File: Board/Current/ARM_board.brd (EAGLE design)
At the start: 105.2 x 84.8 mm, 157 parts, among them IC3 STM32F437VI, IC4 LM358DT, J1 USART/I2C, J10 ANALOG, J11 DGND, J12 DPWR, J13 DIGITAL, J14 SGND, J15 SPWR, J16 SERVO, J2 I2C2/USART3, J3 USART2, J5 SPI, J6 Bluesmirf, J7 SWD, J8 AGND, J9 APWR, Q1 STL4P2UH7, Q2 2STR1230, SW1 SW, U1 LSM330DLC, U10 BAV99, U11 BAV99, U12 USBLC6-2, U13 USBLC6-2, U14 STMPS2171MTR, U15 MC74HC164, U16 STL85N6F3, U17 ZENER-BZX384C20-E3-08, U18 ZENER-BZX384C20-E3-08, U2 RT7259, U3 NC7SZU04, U4 L6206Q, U5 L6206Q, U6 SI7617, U7 SI7617, U8 SI7617, U9 SI7617, Y2 8MHz

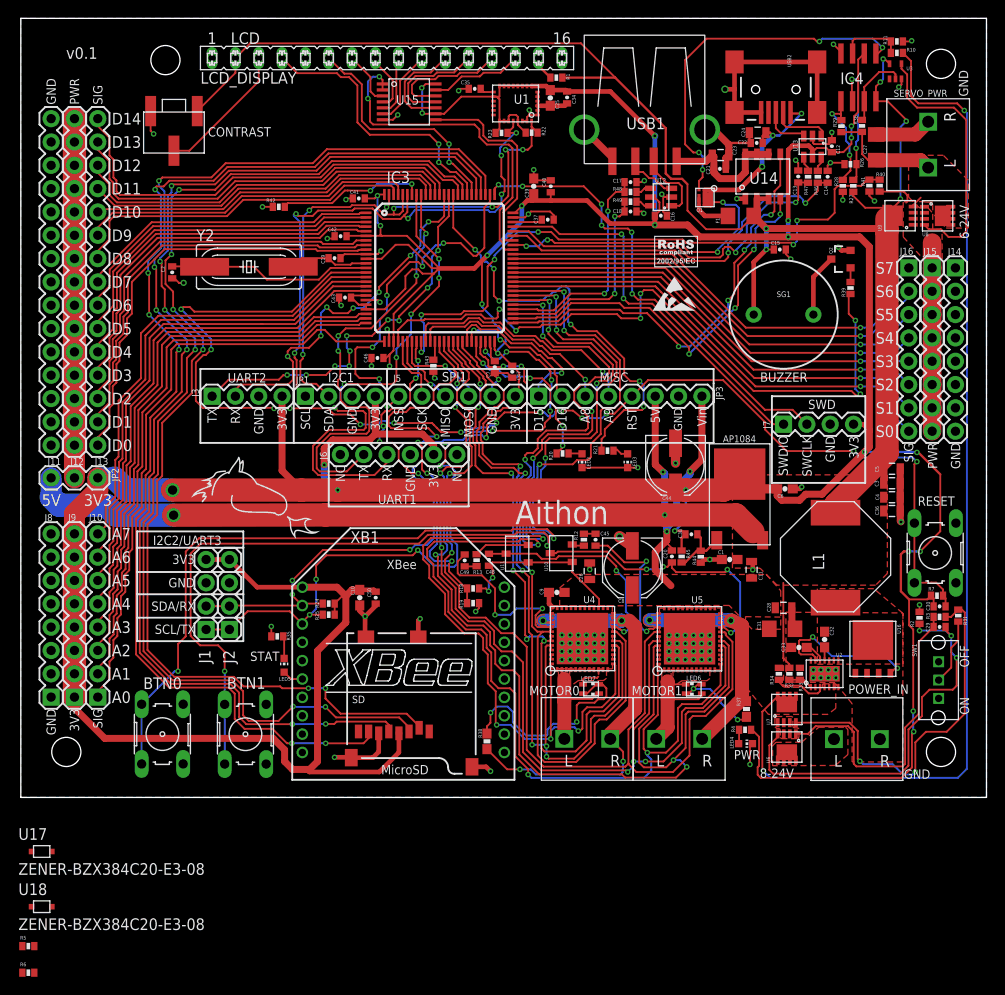
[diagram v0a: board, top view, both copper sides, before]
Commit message: Added green box 30mil inside the board outline and moved all traces within the line. Removed the extra space that was added around the board for the previous revision. Removed the zener diodes for now (need to re-evaluate them).
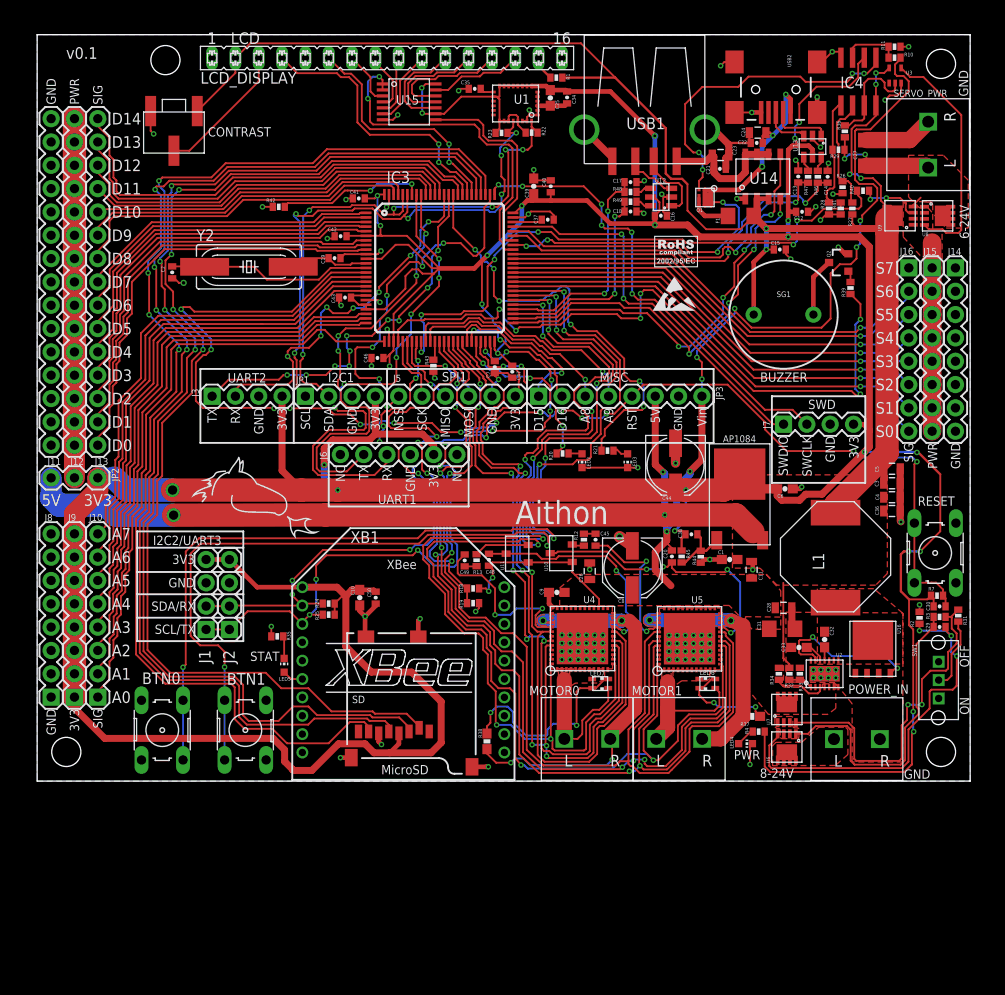
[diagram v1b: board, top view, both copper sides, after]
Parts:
- removed R5, R6: 10k, SparkFun:0402-RES
- removed U17, U18: ZENER-BZX384C20-E3-08, zener-BZX384C20-E3-08:ZENER-BZX384C20-E3-08
- moved C12 7.84 mm to (83.3, 62.0), turned to 0 degrees
- moved R41 3.99 mm to (87.5, 62.4)
- moved R28 2.88 mm to (86.2, 62.4)
- moved R26 2.65 mm to (87.7, 64.7), turned to 90 degrees
- moved R29 2.59 mm to (87.3, 68.8), turned to 180 degrees
- moved R27 2.47 mm to (88.8, 62.4)
- moved R36 1.95 mm to (88.0, 70.8)
- moved R40 1.89 mm to (89.9, 64.3), turned to 180 degrees
- moved LED6 1.58 mm to (73.0, 10.6)
- moved R4 1.50 mm to (78.6, 5.39)
- moved C27 1.24 mm to (90.3, 68.4)
- moved LED7 1.15 mm to (61.3, 10.6)
- moved R37 1.02 mm to (77.9, 7.05), turned to 0 degrees
- moved R11 0.63 mm to (93.4, 80.0)
- moved R10 0.58 mm to (93.4, 78.8)
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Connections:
- net GND: no longer R5.2, R6.2
- net N$30: no longer R6.1, U17.P$2
- net RAW_SPWR: no longer R5.1, U18.P$2
- net SPWR: no longer U17.P$1, U18.P$1
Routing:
- net MPOWER: track 159.5 -> 105.5 mm, vias 6 -> 9
- net GND: track 158.9 -> 140.2 mm, vias 105 -> 109
- net M0_B: track 112.6 -> 106.7 mm
- net +3V3: track 557.9 -> 563.5 mm
- net N$14: track 39.6 -> 34.7 mm
- net N$68: track 40.7 -> 37.0 mm
- net N$30: track 28.9 -> 25.7 mm
- net N$27: track 8.39 -> 11.5 mm
- net SPWR: track 24.6 -> 27.4 mm, vias 0 -> 2
- net OUT4: track 46.2 -> 43.6 mm
- net BTN0: track 111.2 -> 108.6 mm
- net SERVO_SENSE: track 68.4 -> 66.2 mm
- net OUT1: track 14.1 -> 16.2 mm
- net N$52: track 24.7 -> 22.7 mm
- net USB_5V: track 55.9 -> 57.8 mm
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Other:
- board size 105.2 x 84.8 mm -> 101.6 x 81.3 mm

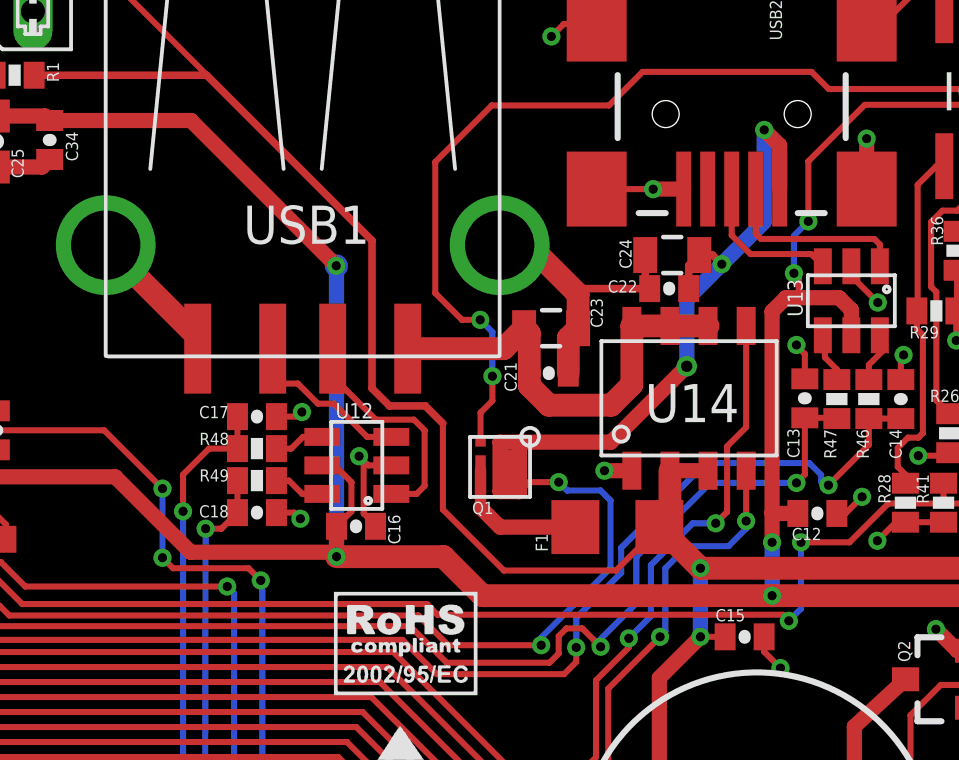
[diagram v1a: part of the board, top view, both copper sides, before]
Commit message: Fixed parts that were too close together.
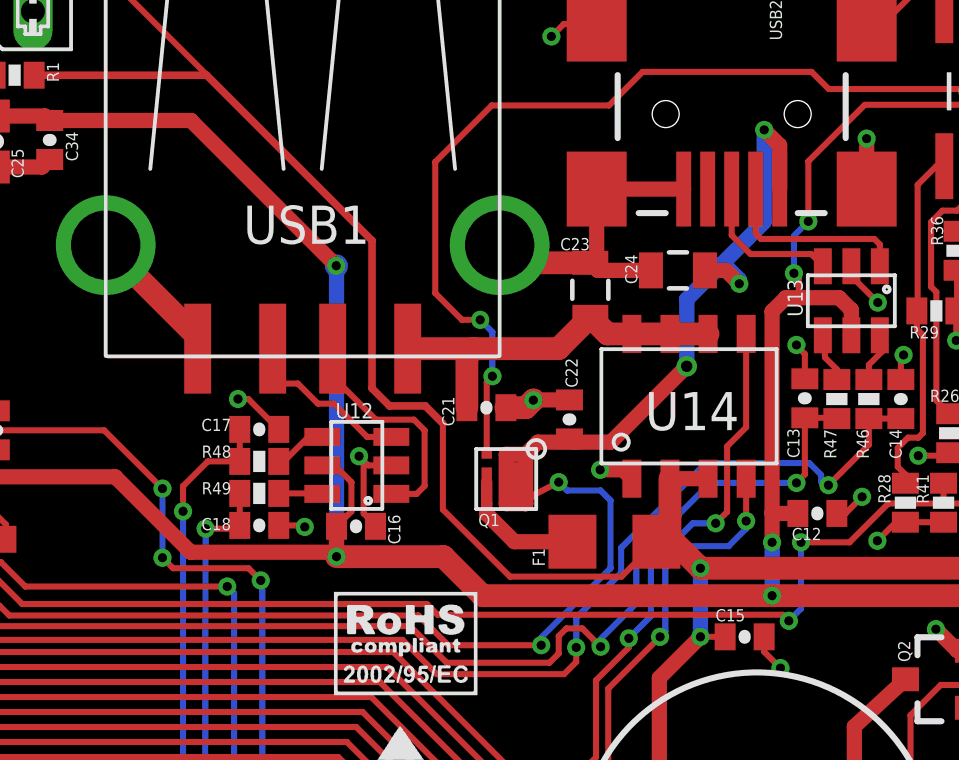
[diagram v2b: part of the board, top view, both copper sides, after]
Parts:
- moved C22 5.48 mm to (75.0, 65.1), turned to 270 degrees
- moved C21 2.38 mm to (72.3, 65.5)
- moved C23 1.83 mm to (75.7, 69.5), turned to 90 degrees
- moved C24 0.54 mm to (78.7, 70.1)
- moved F1 0.50 mm to (75.3, 58.5)
- moved Q1 0.45 mm to (72.9, 63.1)
- moved R49 0.43 mm to (64.7, 62.7)
- moved C17 0.43 mm to (64.7, 64.8)
- moved C18 0.43 mm to (64.7, 61.6)
- moved R48 0.43 mm to (64.7, 63.7)
- moved U14 0.27 mm to (78.4, 64.9)
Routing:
- net N$21: track 14.6 -> 12.8 mm
- net GND: track 140.2 -> 141.8 mm

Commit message: Changed servo power select resistors.
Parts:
- added R5, R6: 100k, SparkFun:0402-RES
- R36: value 10k -> 100k
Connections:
- new net N$50: R5.2, U9.4
- new net N$53: R6.1, U8.4
- net N$30: now also R6.2; no longer U8.4
- net RAW_SPWR: now also R5.1; no longer U9.4
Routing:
- net RAW_SPWR: track 14.2 -> 12.9 mm
- net N$30: track 25.7 -> 25.1 mm
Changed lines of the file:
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@@
 <layer number="39" name="tKeepout" color="4" fill="11" visible="no" active="yes"/>
 <layer number="40" name="bKeepout" color="1" fill="11" visible="no" active="yes"/>
-<layer number="41" name="tRestrict" color="4" fill="10" visible="no" active="yes"/>
+<layer number="41" name="tRestrict" color="4" fill="10" visible="yes" active="yes"/>
 <layer number="42" name="bRestrict" color="1" fill="10" visible="no" active="yes"/>
 <layer number="43" name="vRestrict" color="2" fill="10" visible="yes" active="yes"/>
@@
 <wire x1="100.838" y1="0.762" x2="0.762" y2="0.762" width="0" layer="43"/>
 <wire x1="0.762" y1="0.762" x2="0.762" y2="80.518" width="0" layer="43"/>
+<wire x1="1.27" y1="80.01" x2="100.33" y2="80.01" width="0" layer="43"/>
+<wire x1="100.33" y1="80.01" x2="100.33" y2="1.27" width="0" layer="43"/>
+<wire x1="100.33" y1="1.27" x2="1.27" y2="1.27" width="0" layer="43"/>
+<wire x1="1.27" y1="1.27" x2="1.27" y2="80.01" width="0" layer="43"/>
 </plain>
 <attributes>
@@
 <attribute name="VALUE" x="99.710240625" y="18.912840625" size="0.4064" layer="27" font="vector" rot="R90"/>
 </element>
-<element name="R36" library="SparkFun" package="0402-RES" value="10k" x="87.955121875" y="70.754240625" smashed="yes" rot="R270">
+<element name="R36" library="SparkFun" package="0402-RES" value="100k" x="87.955121875" y="70.754240625" smashed="yes" rot="R270">
 <attribute name="NAME" x="87.4903" y="70.926959375" size="0.4064" layer="25" font="vector" rot="R90"/>
 <attribute name="VALUE" x="87.5385625" y="71.78548125" size="0.4064" layer="27" font="vector"/>
@@
 <attribute name="VALUE" x="48.674021875" y="5.80644375" size="0.4064" layer="27" font="vector"/>
 </element>
+<element name="R5" library="SparkFun" package="0402-RES" value="100k" x="-0.96011875" y="-13.738859375"/>
+<element name="R6" library="SparkFun" package="0402-RES" value="100k" x="-0.96011875" y="-16.634459375"/>
 </elements>
 <signals>
@@
 <contactref element="SERVO_PWR" pad="L"/>
 <contactref element="R36" pad="2"/>
-<contactref element="U9" pad="4"/>
-<contactref element="U8" pad="5"/>
-<contactref element="U8" pad="6"/>
-<contactref element="U8" pad="7"/>
-<contactref element="U8" pad="8"/>
-<contactref element="U8" pad="PAD"/>
 <polygon width="0.0254" layer="1" thermals="no" rank="2">
 <vertex x="94.8944" y="68.1482"/>
@@
 <vertex x="98.679" y="68.1482"/>
 </polygon>
-<wire x1="95.4024" y1="62.5602" x2="95.4024" y2="62.7253" width="0.2032" layer="1"/>
-<wire x1="95.4024" y1="62.7253" x2="96.2152" y2="63.5381" width="0.2032" layer="1"/>
 <wire x1="90.289378125" y1="67.002196875" x2="96.831603125" y2="67.002196875" width="1.778" layer="1"/>
 <wire x1="96.831603125" y1="67.002196875" x2="97.028" y2="66.8058" width="1.778" layer="1"/>
@@
 <wire x1="87.92718125" y1="67.764659375" x2="87.92718125" y2="68.737234375" width="0.2032" layer="1"/>
 <wire x1="87.92718125" y1="68.737234375" x2="87.9142375" y2="68.750178125" width="0.2032" layer="1"/>
+<contactref element="U8" pad="PAD"/>
+<contactref element="U8" pad="7"/>
+<contactref element="U8" pad="6"/>
+<contactref element="U8" pad="5"/>
+<contactref element="U8" pad="8"/>
+<contactref element="R5" pad="1"/>
+<wire x1="87.92718125" y1="67.764659375" x2="-1.61011875" y2="-13.738859375" width="0" layer="19" extent="1-16"/>
 </signal>
 <signal name="N$27">
@@
 <signal name="N$30">
 <contactref element="U3" pad="4"/>
-<contactref element="U8" pad="4"/>
 <wire x1="98.5901" y1="60.0964" x2="97.0915" y2="60.0964" width="0.2032" layer="1"/>
-<wire x1="97.0915" y1="60.0964" x2="96.6216" y2="60.5663" width="0.2032" layer="1"/>
 <wire x1="95.071459375" y1="76.672440625" x2="96.5073" y2="76.672440625" width="0.2032" layer="1"/>
 <wire x1="95.071459375" y1="76.672440625" x2="94.0839" y2="77.66" width="0.2032" layer="1"/>
@@
 <wire x1="100.637340625" y1="59.99988125" x2="100.637340625" y2="72.5424" width="0.2032" layer="1"/>
 <wire x1="100.637340625" y1="72.5424" x2="96.5073" y2="76.672440625" width="0.2032" layer="1"/>
+<contactref element="R6" pad="2"/>
+<wire x1="-0.31011875" y1="-16.634459375" x2="97.0915" y2="60.0964" width="0" layer="19" extent="1-1"/>
 </signal>
 <signal name="N$44">
@@
 <wire x1="55.8546" y1="46.504859375" x2="54.9783" y2="47.381159375" width="0.2032" layer="1"/>
 </signal>
+<signal name="N$50">
+<contactref element="R5" pad="2"/>
+<contactref element="U9" pad="4"/>
+<wire x1="-0.31011875" y1="-13.738859375" x2="95.4024" y2="62.5602" width="0" layer="19" extent="1-1"/>
+</signal>
+<signal name="N$53">
+<contactref element="R6" pad="1"/>
+<contactref element="U8" pad="4"/>
+<wire x1="-1.61011875" y1="-16.634459375" x2="96.6216" y2="60.5663" width="0" layer="19" extent="1-1"/>
+</signal>
 </signals>
-<errors>
-</errors>
 </board>
 </drawing>
